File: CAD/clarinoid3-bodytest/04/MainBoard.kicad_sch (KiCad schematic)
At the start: 15 parts, among them J12 main header multi to LH, J16 AudioOut, J19 clarinoid3 DAC and POT subboa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, J7 I2C HEADER main to PITCH, J9 OLED_HEADER, U2 APCI0108-P001A Teensy_4.0_Mic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, U3 Micromod outline

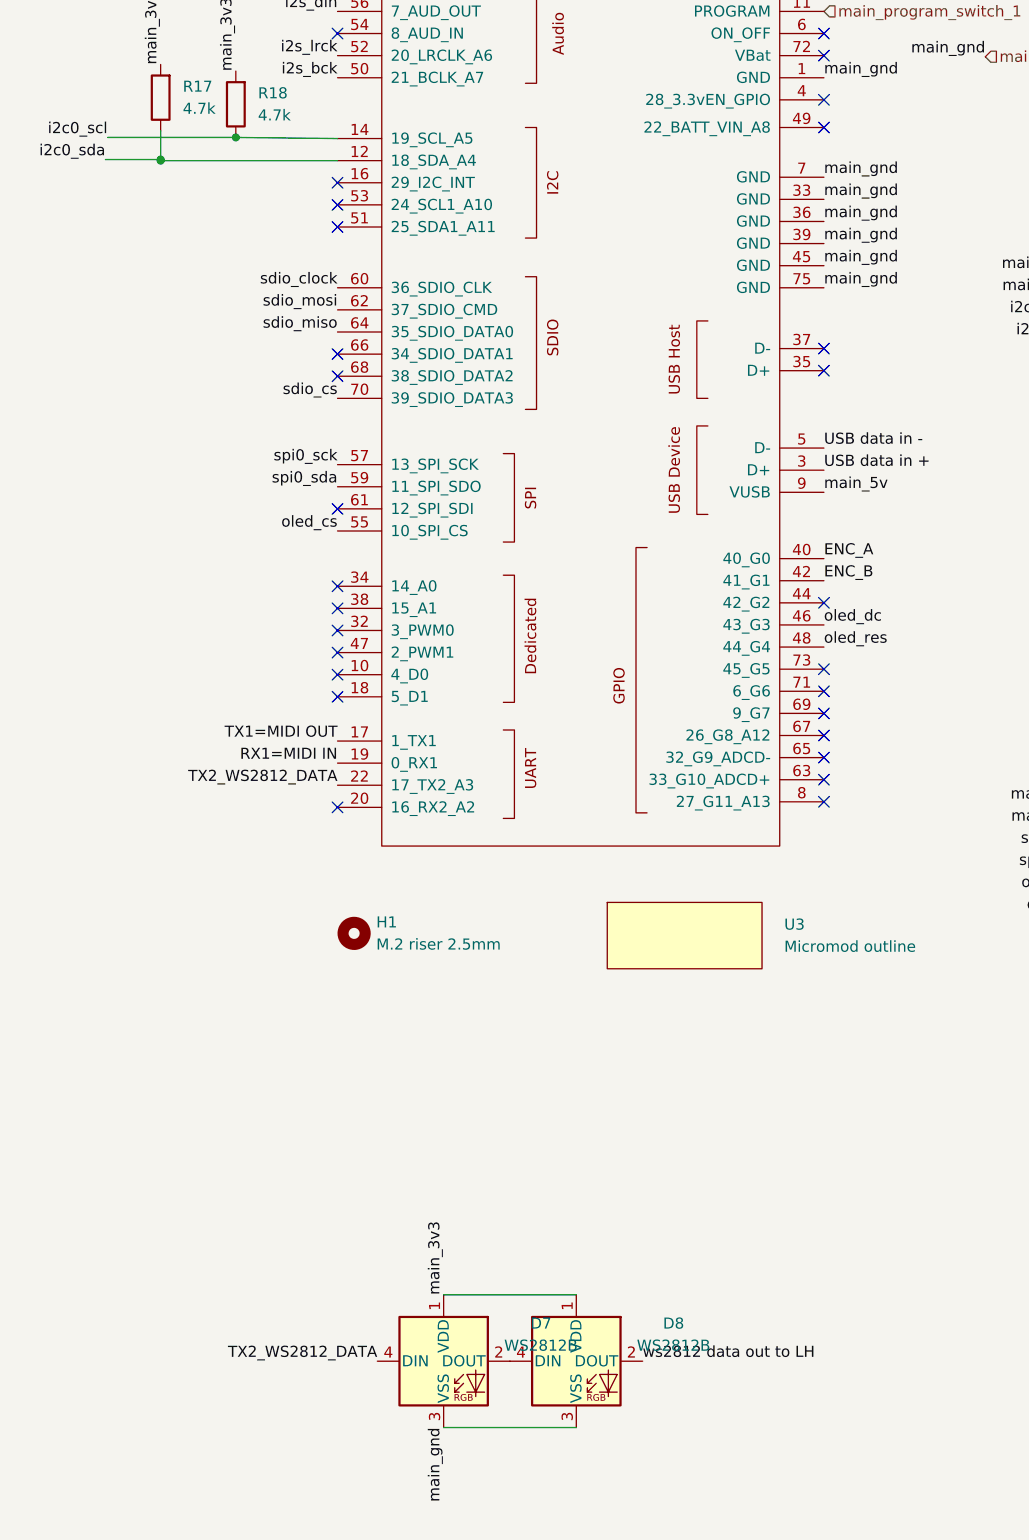
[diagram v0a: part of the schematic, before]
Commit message: c3 design work adding more 3dp tests
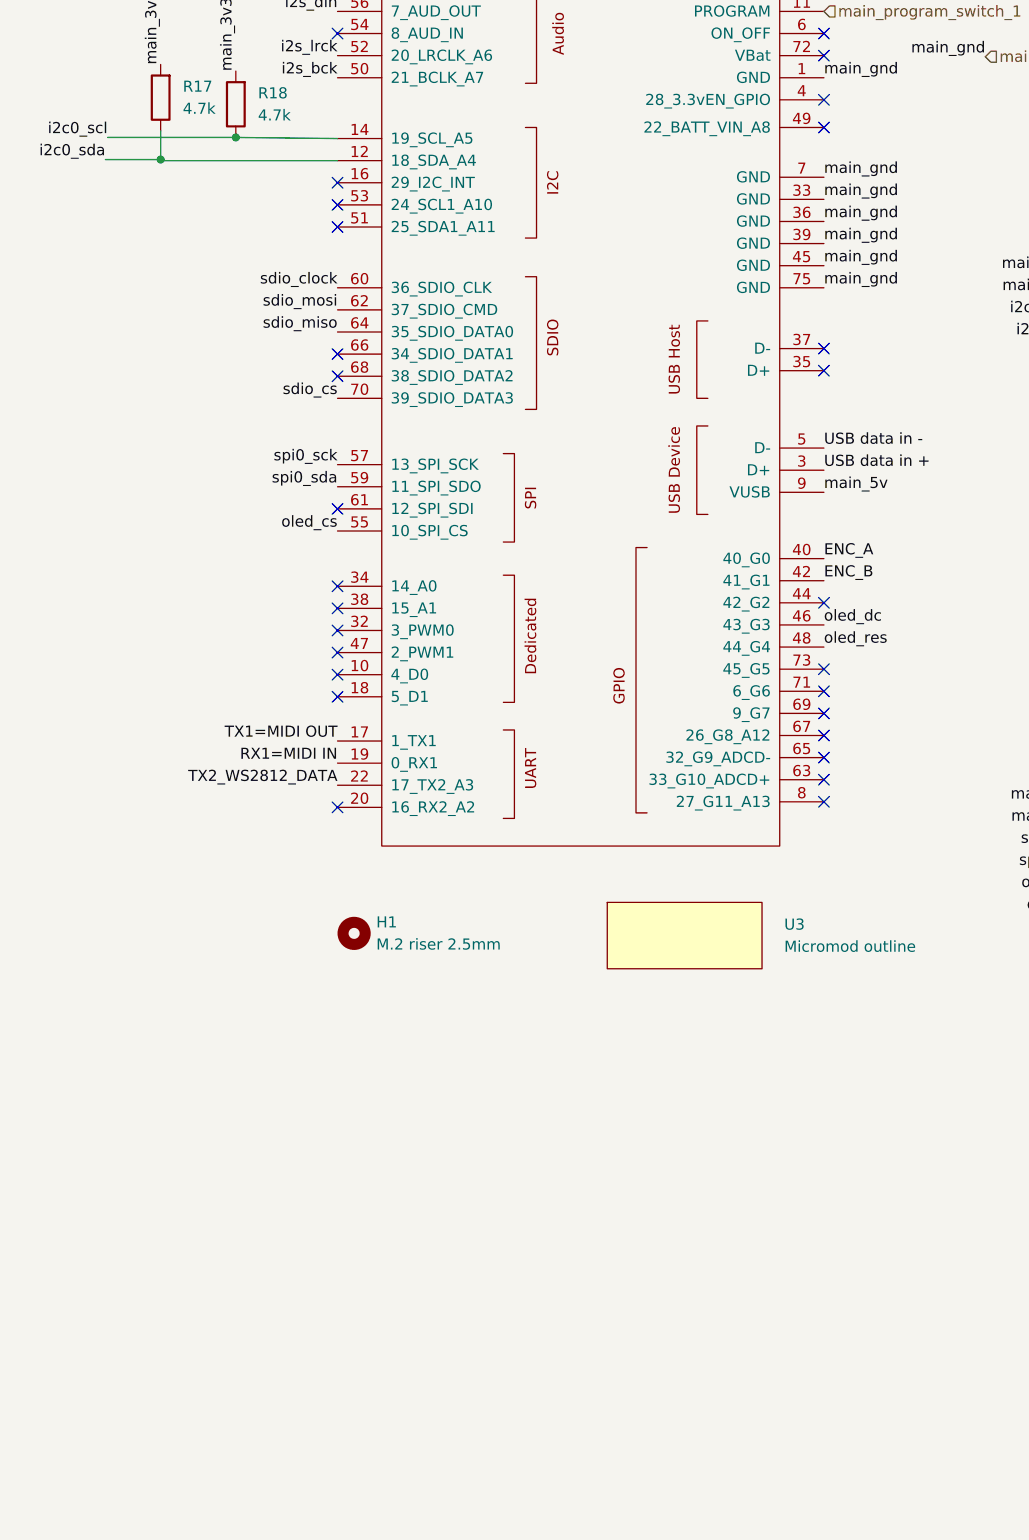
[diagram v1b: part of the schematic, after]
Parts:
- removed D7, D8: WS2812B, LED_SMD:LED_WS2812B_PLCC4_5.0x5.0mm_P3.2mm, symbol LED:WS2812B
